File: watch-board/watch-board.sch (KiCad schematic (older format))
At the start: 4 parts

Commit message: setting up linear voltage regulator at 3.1V
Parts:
- removed Q?: Transistor-BJT_MMBT3904-TP, Package_TO_SOT_SMD:SOT-23, symbol luke:Transistor-BJT_MMBT3904-TP
- added C?: C_4.7uF, Capacitor_SMD:C_1206_3216Metric, symbol luke:C_4.7uF
- added C?: C_7pF, Capacitor_SMD:C_0805_2012Metric, symbol luke:C_7pF
- added C?: C_1uF, Capacitor_SMD:C_0805_2012Metric, symbol luke:C_1uF
- added Q?: Transistor_MMBT3904-TP, Package_TO_SOT_SMD:SOT-23, symbol luke:Transistor_MMBT3904-TP
- added R?: R_51.1K, Resistor_SMD:R_0805_2012Metric, symbol luke:R_51.1K
- added R?: R_78.7K, Resistor_SMD:R_0805_2012Metric, symbol luke:R_78.7K
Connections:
- net labels added: GND
- wire segments 0 -> 15
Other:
- note added: "Vout = Vref + (Vref * (Radj/51.1K))\nVref Typical = 1.225 (min = 1.213 max = 1.237)\nRadj = 78.7K\nVout =3.11\n3.08 < Vout < 3.14"
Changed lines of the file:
@@
 $EndComp
 $Comp
-L luke:Transistor-BJT_MMBT3904-TP Q?
-U 1 1 5EA1FA57
-P 5250 4500
-F 0 "Q?" H 5440 4546 50  0000 L CNN
-F 1 "Transistor-BJT_MMBT3904-TP" H 5440 4455 50  0000 L CNN
-F 2 "Package_TO_SOT_SMD:SOT-23" H 5450 4425 50  0001 L CIN
-F 3 "https://www.mccsemi.com/pdf/Products/MMBT3904(SOT-23).pdf" H 5250 4500 50  0001 L CNN
-F 4 "https://www.digikey.com/product-detail/en/micro-commercial-co/MMBT3904-TP/MMBT3904TPMSCT-ND/717395" H 5250 4500 50  0001 L CNN "Purchasing Link"
-F 5 "MMBT3904TPMSCT-ND " H 5250 4500 50  0001 L CNN "Digi-Key_PN"
-	1    5250 4500
+L luke:Transistor_MMBT3904-TP Q?
+U 1 1 5EA32A90
+P 5350 4400
+F 0 "Q?" H 5540 4446 50  0000 L CNN
+F 1 "Transistor_MMBT3904-TP" H 5540 4355 50  0000 L CNN
+F 2 "Package_TO_SOT_SMD:SOT-23" H 5550 4300 50  0001 L CIN
+F 3 "https://www.mccsemi.com/pdf/Products/MMBT3904(SOT-23).pdf" H 5350 4400 50  0001 L CNN
+F 4 "https://www.digikey.com/product-detail/en/micro-commercial-co/MMBT3904-TP/MMBT3904TPMSCT-ND/717395" H 5550 4200 50  0001 L CNN "Purchasing Link"
+F 5 "MMBT3904TPMSCT-ND " H 5550 4100 50  0001 L CNN "Digi-Key_PN"
+	1    5350 4400
 	1    0    0    -1
 $EndComp
+$Comp
+L luke:C_4.7uF C?
+U 1 1 5EA337B8
+P 7700 1550
+F 0 "C?" H 7815 1596 50  0000 L CNN
+F 1 "C_4.7uF" H 7815 1505 50  0000 L CNN
+F 2 "Capacitor_SMD:C_1206_3216Metric" H 7700 900 50  0001 C CNN
+F 3 "http://datasheets.avx.com/TAJ.pdf" H 7725 1650 50  0001 C CNN
+F 4 "478-3868-2-ND " H 7700 1000 60  0001 C CNN "Digi-Key_PN"
+F 5 "https://www.digikey.com/product-detail/en/avx-corporation/TAJA475K016RNJ/478-3868-2-ND/1126796" H 7700 800 60  0001 C CNN "Purchasing Link"
+	1    7700 1550
+	1    0    0    -1
+$EndComp
+$Comp
+L power:GND #PWR?
+U 1 1 5EA36173
+P 7700 1700
+F 0 "#PWR?" H 7700 1450 50  0001 C CNN
+F 1 "GND" H 7705 1527 50  0000 C CNN
+F 2 "" H 7700 1700 50  0001 C CNN
+F 3 "" H 7700 1700 50  0001 C CNN
+	1    7700 1700
+	1    0    0    -1
+$EndComp
+$Comp
+L luke:C_7pF C?
+U 1 1 5EA3DC50
+P 7200 1550
+F 0 "C?" H 7315 1596 50  0000 L CNN
+F 1 "C_7pF" H 7315 1505 50  0000 L CNN
+F 2 "Capacitor_SMD:C_0805_2012Metric" H 7238 1400 50  0001 C CNN
+F 3 "http://datasheets.avx.com/C0GNP0-Dielectric.pdf" H 7225 1650 50  0001 C CNN
+F 4 "478-10543-1-ND" H 7200 1550 60  0001 C CNN "Digi-Key_PN"
+F 5 "https://www.digikey.com/product-detail/en/avx-corporation/08055A7R0CAT2A/478-10543-1-ND/6797474" H 7625 2050 60  0001 C CNN "Purchasing Link"
+	1    7200 1550
+	1    0    0    -1
+$EndComp
+Text Notes 5450 2900 0    50   ~ 0
+Vout = Vref + (Vref * (Radj/51.1K))\nVref Typical = 1.225 (min = 1.213 max = 1.237)\nRadj = 78.7K\nVout =3.11\n3.08 < Vout < 3.14
+$Comp
+L power:GND #PWR?
+U 1 1 5EA5975A
+P 6600 2100
+F 0 "#PWR?" H 6600 1850 50  0001 C CNN
+F 1 "GND" H 6605 1927 50  0000 C CNN
+F 2 "" H 6600 2100 50  0001 C CNN
+F 3 "" H 6600 2100 50  0001 C CNN
+	1    6600 2100
+	1    0    0    -1
+$EndComp
+$Comp
+L luke:R_51.1K R?
+U 1 1 5EA4966E
+P 6600 1950
+F 0 "R?" H 6670 1996 50  0000 L CNN
+F 1 "R_51.1K" H 6670 1905 50  0000 L CNN
+F 2 "Resistor_SMD:R_0805_2012Metric" H 5500 2250 50  0001 L CNN
+F 3 "https://industrial.panasonic.com/cdbs/www-data/pdf/RDA0000/AOA0000C304.pdf" H 5500 2350 50  0001 L CNN
+F 4 "P51.1KCCT-ND" H 5500 2150 60  0001 L CNN "Digi-Key_PN"
+F 5 "https://www.digikey.com/product-detail/en/panasonic-electronic-components/ERJ-6ENF5112V/P51.1KCCT-ND/119466" H 5500 2450 60  0001 L CNN "Purchasing Link"
+	1    6600 1950
+	1    0    0    -1
+$EndComp
+$Comp
+L luke:R_78.7K R?
+U 1 1 5EA619B4
+P 6600 1550
+F 0 "R?" H 6670 1596 50  0000 L CNN
+F 1 "R_78.7K" H 6670 1505 50  0000 L CNN
+F 2 "Resistor_SMD:R_0805_2012Metric" H 5500 1850 50  0001 L CNN
+F 3 "https://www.yageo.com/upload/media/product/productsearch/datasheet/rchip/PYu-RC_Group_51_RoHS_L_10.pdf" H 5500 1950 50  0001 L CNN
+F 4 "311-78.7KCRCT-ND " H 5500 1750 60  0001 L CNN "Digi-Key_PN"
+F 5 "https://www.digikey.com/product-detail/en/yageo/RC0805FR-0778K7L/311-78-7KCRCT-ND/731088" H 5500 2050 60  0001 L CNN "Purchasing Link"
+	1    6600 1550
+	1    0    0    -1
+$EndComp
+Wire Wire Line
+	6600 1700 6600 1750
+Wire Wire Line
+	6600 1750 6350 1750
+Wire Wire Line
+	6350 1450 6300 1450
+Wire Wire Line
+	6600 1750 6600 1800
+Connection ~ 6600 1750
+Wire Wire Line
+	7200 1700 7200 1750
+Wire Wire Line
+	7200 1750 6600 1750
+Wire Wire Line
+	6300 1350 6600 1350
+Wire Wire Line
+	6350 1450 6350 1750
+Wire Wire Line
+	6600 1400 6600 1350
+Connection ~ 6600 1350
+Wire Wire Line
+	6600 1350 7200 1350
+Wire Wire Line
+	7200 1350 7200 1400
+Wire Wire Line
+	7200 1350 7700 1350
+Wire Wire Line
+	7700 1350 7700 1400
+Connection ~ 7200 1350
+$Comp
+L power:GND #PWR?
+U 1 1 5EA7CD31
+P 5900 1750
+F 0 "#PWR?" H 5900 1500 50  0001 C CNN
+F 1 "GND" H 5905 1577 50  0000 C CNN
+F 2 "" H 5900 1750 50  0001 C CNN
+F 3 "" H 5900 1750 50  0001 C CNN
+	1    5900 1750
+	1    0    0    -1
+$EndComp
+$Comp
+L luke:C_1uF C?
+U 1 1 5EA86DAA
+P 4900 1600
+F 0 "C?" H 5015 1696 50  0000 L CNN
+F 1 "C_1uF" H 5015 1605 50  0000 L CNN
+F 2 "Capacitor_SMD:C_0805_2012Metric" H 4938 2200 50  0001 C CNN
+F 3 "https://www.yageo.com/upload/media/product/productsearch/datasheet/mlcc/UPY-GPHC_Y5V_6.3V-to-50V_9.pdf" H 4925 2450 50  0001 C CNN
+F 4 "https://www.digikey.com/product-detail/en/yageo/CC0805ZKY5V9BB105/311-1909-1-ND/5195811#images" H 5325 2100 60  0001 C CNN "Purchasing Link"
+F 5 "311-1909-1-ND " H 4900 2300 50  0001 C CNN "Digi-Key_PN"
+	1    4900 1600
+	1    0    0    -1
+$EndComp
+Wire Wire Line
+	5500 1350 4900 1350
+Wire Wire Line
+	4900 1350 4900 1400
+$Comp
+L power:GND #PWR?
+U 1 1 5EA88D89
+P 4900 1700
+F 0 "#PWR?" H 4900 1450 50  0001 C CNN
+F 1 "GND" H 4905 1527 50  0000 C CNN
+F 2 "" H 4900 1700 50  0001 C CNN
+F 3 "" H 4900 1700 50  0001 C CNN
+	1    4900 1700
+	1    0    0    -1
+$EndComp

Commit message: adding battery and solar cell
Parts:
- added BT?: BAT_ML2020, symbol luke:BAT_ML2020
- added D? (x2): D-Schotkey_BAT54HT1G, Diode_SMD:D_SOD-323, symbol luke:D-Schotkey_BAT54HT1G
- added R?: R_160, Resistor_SMD:R_0805_2012Metric, symbol luke:R_160
- added R?: R_2.21M, Resistor_SMD:R_0805_2012Metric, symbol luke:R_2.21M
- added SC?: Solar-Cells_KXOB25-02X8F, symbol luke:Solar-Cells_KXOB25-02X8F
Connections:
- net labels added: VCC, V_BAT, V_Charge
- wire segments 15 -> 30
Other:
- note added: "Calcular ESR is 886Ohms\n160Ohm resistor used for current limiting durring charging"
- moved on the sheet: C?, R?, U?

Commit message: power management desgin complete
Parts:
- removed Q?: Transistor_MMBT3904-TP, Package_TO_SOT_SMD:SOT-23, symbol luke:Transistor_MMBT3904-TP
- removed R?: R_2.21M, Resistor_SMD:R_0805_2012Metric, symbol luke:R_2.21M
- added D?: D-Schotkey_BAT54HT1G, Diode_SMD:D_SOD-323, symbol luke:D-Schotkey_BAT54HT1G
- added Q?: Transistor_FZT796ATA, Package_TO_SOT_SMD:SOT-223, symbol luke:Transistor_FZT796ATA
- added R?: R_100K, Resistor_SMD:R_0805_2012Metric, symbol luke:R_100K
- added R?: R_200K, Resistor_SMD:R_0805_2012Metric, symbol luke:R_200K
- added R?: R_1.2M, Resistor_SMD:R_0805_2012Metric, symbol luke:R_1.2M
- added R?: R_49.9K, Resistor_SMD:R_0805_2012Metric, symbol luke:R_49.9K
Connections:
- net labels added: V_Charge_ON
- wire segments 30 -> 46
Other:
- note added: "Rt = 1500000 (high value for low current draw)\nR3 = (Rt/Vo)*Vi\nR2 = ((Rt/Vu)*(Vi-Vhys))-R3\nR1 = Rt - R2 - R3\nVi = 0.4V\nVo = 3V\nVu = 2V\nVhys = 5.5mV [(Vi+) - (Vi-)]\n\nR2 =95875 (rounding up to 100K for convience)\nR3 = 200K"
- moved on the sheet: BT?, C?, D?, R?, SC?, U?

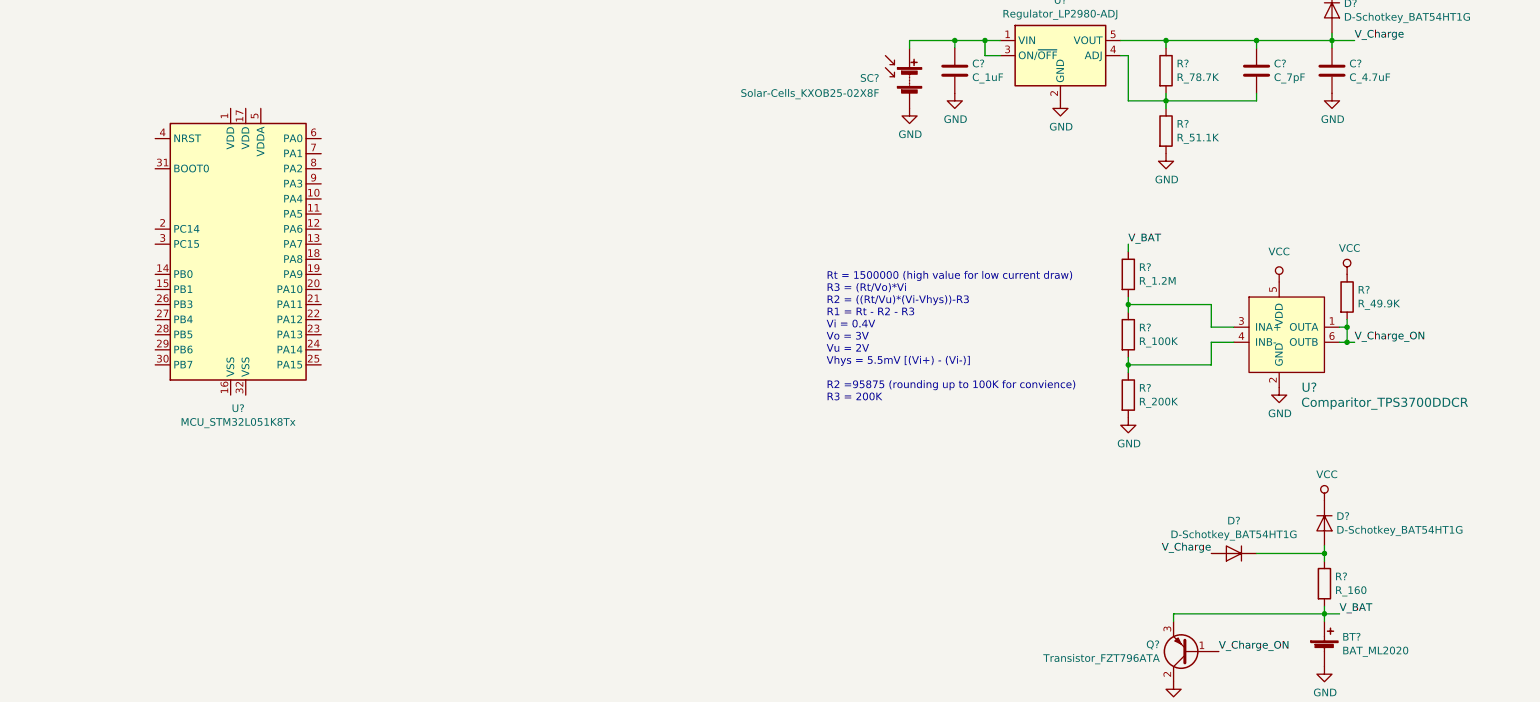
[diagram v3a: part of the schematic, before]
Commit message: adding bypass caps to STM32
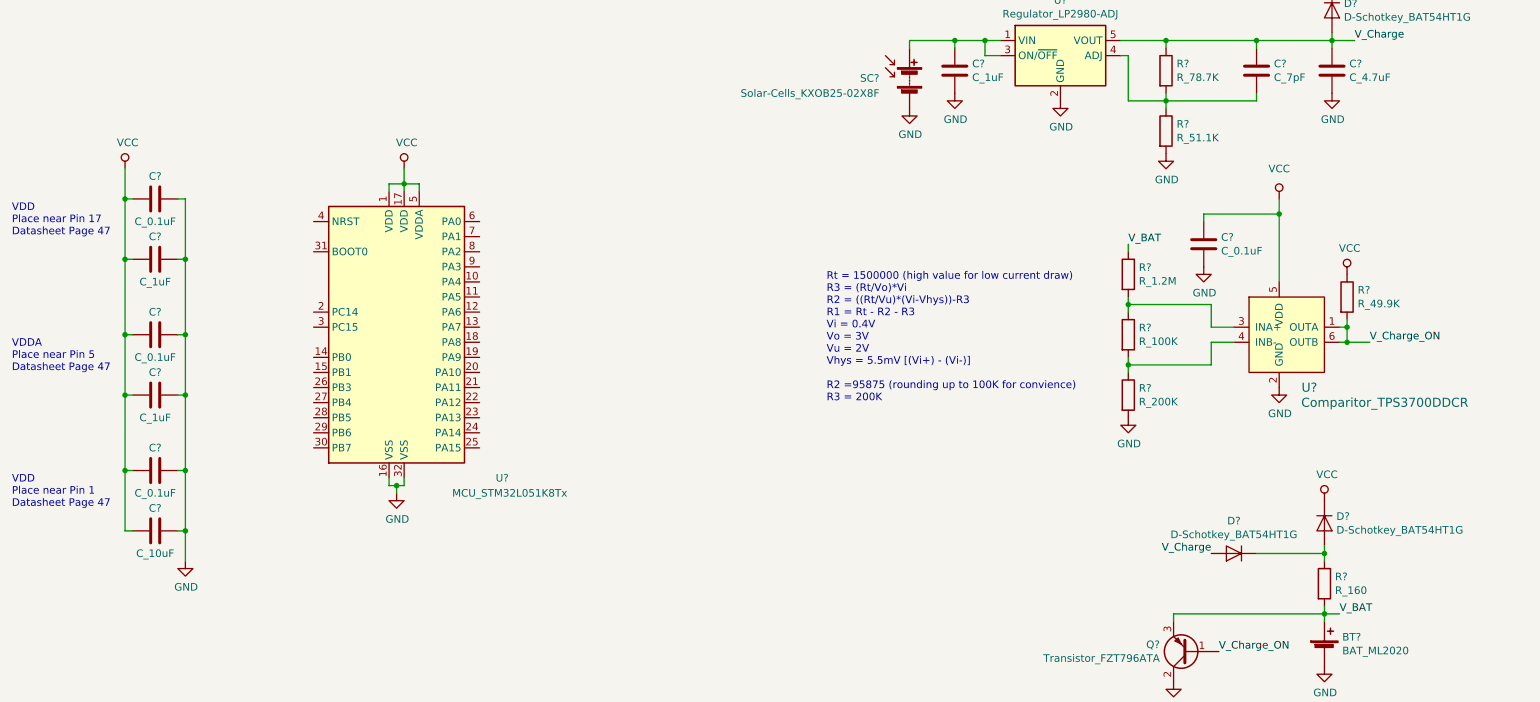
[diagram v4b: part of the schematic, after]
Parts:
- added C? (x4): C_0.1uF, Capacitor_SMD:C_0805_2012Metric, symbol luke:C_0.1uF
- added C? (x2): C_1uF, Capacitor_SMD:C_0805_2012Metric, symbol luke:C_1uF
- added C?: C_10uF, Capacitor_SMD:C_0805_2012Metric, symbol luke:C_10uF
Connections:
- net GND: now also U?.16 (VSS), U?.32 (VSS), C?.1, C?.1, C?.1, C?.1, C?.1, C?.1, C?.1
- net VCC: now also U?.1 (VDD), U?.17 (VDD), U?.5 (VDDA), C?.2, C?.2, C?.2, C?.2, C?.2, C?.2, C?.2
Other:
- note added: "VDDA\nPlace near Pin 5\nDatasheet Page 47"
- note added: "VDD\nPlace near Pin 17\nDatasheet Page 47"
- note added: "VDD\nPlace near Pin 1\nDatasheet Page 47"
- moved on the sheet: U?

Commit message: adding TODOs
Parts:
- added C?: C_0.1uF, Capacitor_SMD:C_0805_2012Metric, symbol luke:C_0.1uF
- added J?: Conn_01x05_Male, Connector_PinHeader_2.54mm:PinHeader_1x05_P2.54mm_Vertical, symbol luke:Conn_01x05_Male
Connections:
- net GND: now also U?.31 (BOOT0), C?.2, J?.4 (Pin_4)
- net VCC: no longer C?.2, C?.2, C?.2, C?.2, C?.2, C?.2, C?.2, R?.1, U?.1 (VDD), U?.17 (VDD), U?.5 (VDD), U?.5 (VDDA)
- net V_BAT: no longer Q?.3 (E)
- net V_Charge: now also Q?.3 (E), R?.1
- net SWDIO: now reaches U?.23 (PA13)
- net SWDIO: now also J?.3 (Pin_3)
- net SWCLK: now reaches U?.24 (PA14)
- net SWCLK: now also J?.2 (Pin_2)
- net RST: now reaches U?.4 (NRST)
- net RST: now also C?.1, J?.1 (Pin_1)
- new net VDD: C?.2, C?.2, C?.2, C?.2, C?.2, C?.2, C?.2, J?.5 (Pin_5), U?.1 (VDD), U?.17 (VDD), U?.5 (VDD), U?.5 (VDDA)
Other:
- note added: "Add SPI Pins"
- note added: "use BUCK-BOOST (TPS6305) to set VDD to 3V"
- moved on the sheet: C?, D?, Q?, R?, SC?, U?

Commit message: adding more TODOs
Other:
- note added: "TODO: Add SPI Pins"
- note removed: "Add SPI Pins"
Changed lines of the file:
@@
 $EndComp
 Text Notes 5500 5450 0    50   ~ 0
-Add SPI Pins
+TODO: Add SPI Pins
 $EndSCHEMATC

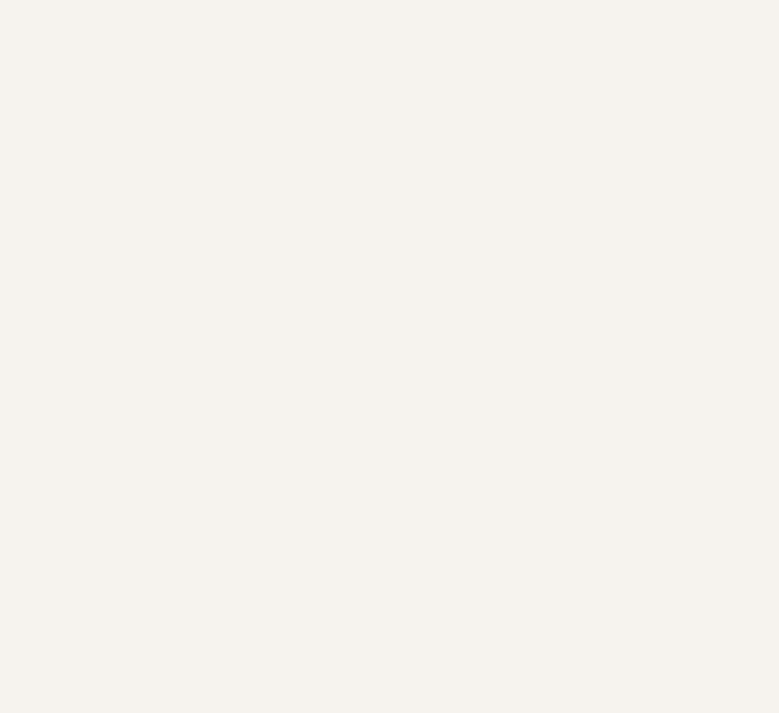
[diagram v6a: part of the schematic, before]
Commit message: switching to LTC3105 for power harvesting
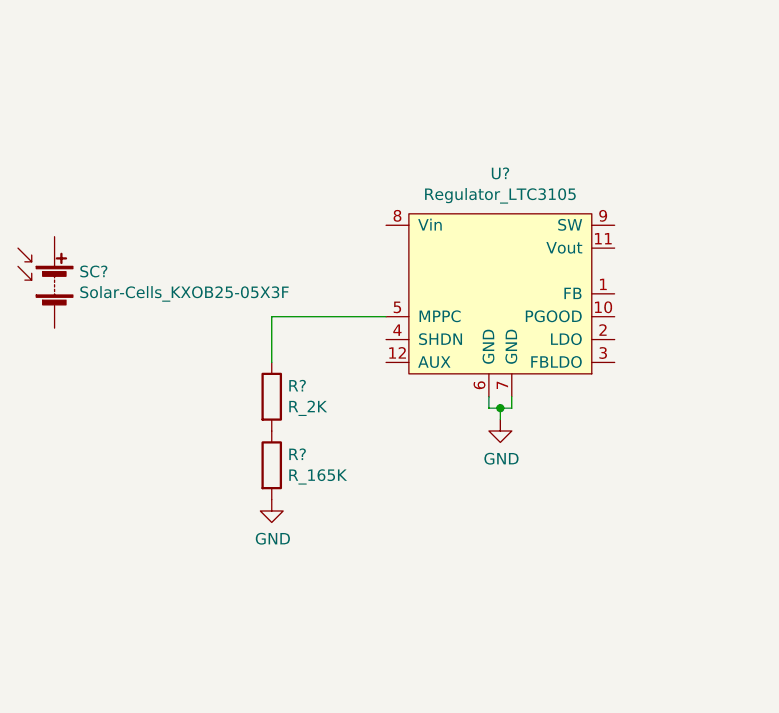
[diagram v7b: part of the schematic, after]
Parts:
- added R?: R_2K, Resistor_SMD:R_0805_2012Metric, symbol luke:R_2K
- added R?: R_165K, Resistor_SMD:R_0805_2012Metric, symbol luke:R_165K
- added SC?: Solar-Cells_KXOB25-05X3F, symbol luke:Solar-Cells_KXOB25-05X3F
- added U?: Regulator_LTC3105, Digikey-footprints:MSOP-12-1EP_W3mm, symbol luke:Regulator_LTC3105
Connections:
- net GND: now also R?.2, U?.6 (GND), U?.7 (GND)
- new net: R?.1, U?.5 (MPPC)
- new net: R?.1, R?.2
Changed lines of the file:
@@
 Text Notes 5500 5450 0    50   ~ 0
 TODO: Add SPI Pins
+$Comp
+L luke:Regulator_LTC3105 U?
+U 1 1 5EBDFA52
+P -3600 2050
+F 0 "U?" H -3600 2575 50  0000 C CNN
+F 1 "Regulator_LTC3105" H -3600 2484 50  0000 C CNN
+F 2 "Digikey-footprints:MSOP-12-1EP_W3mm" H -3600 1150 50  0001 C CNN
+F 3 "https://www.analog.com/media/en/technical-documentation/data-sheets/3105fb.pdf" H -3600 2900 50  0001 C CNN
+F 4 "LTC3105EMS#PBF-ND" H -3600 1350 50  0001 C CNN "Digi-Key_PN"
+F 5 "https://www.digikey.com/product-detail/en/LTC3105EMS%23PBF/LTC3105EMS%23PBF-ND/2601181" H -3600 1250 50  0001 C CNN "Purchasing Link"
+	1    -3600 2050
+	1    0    0    -1
+$EndComp
+$Comp
+L luke:Solar-Cells_KXOB25-05X3F SC?
+U 1 1 5EBE50EA
+P -5550 2000
+F 0 "SC?" H -5442 2046 50  0000 L CNN
+F 1 "Solar-Cells_KXOB25-05X3F" H -5442 1955 50  0000 L CNN
+F 2 "" V -5550 2060 50  0001 C CNN
+F 3 "https://ixapps.ixys.com/DataSheet/KXOB25_05X3F.pdf" V -5550 2060 50  0001 L CNN
+F 4 "KXOB25-05X3FCT-ND" H -5450 1900 50  0001 L CNN "Digi-Key_PN"
+F 5 "https://www.digikey.com/product-detail/en/ixys/KXOB25-05X3F-TR/KXOB25-05X3FCT-ND/9990481" H -5450 1800 50  0001 L CNN "Purchasing Link"
+	1    -5550 2000
+	1    0    0    -1
+$EndComp
+$Comp
+L luke:R_2K R?
+U 1 1 5EBE7BEB
+P -4600 2500
+F 0 "R?" H -4530 2546 50  0000 L CNN
+F 1 "R_2K" H -4530 2455 50  0000 L CNN
+F 2 "Resistor_SMD:R_0805_2012Metric" H -5700 2800 50  0001 L CNN
+F 3 "https://www.yageo.com/upload/media/product/productsearch/datasheet/rchip/PYu-RC_Group_51_RoHS_L_10.pdf" H -5700 2900 50  0001 L CNN
+F 4 "311-2.00KCRCT-ND" H -5700 2700 60  0001 L CNN "Digi-Key_PN"
+F 5 "https://www.digikey.com/product-detail/en/yageo/RC0805FR-072KL/311-2-00KCRCT-ND/730611" H -5700 3000 60  0001 L CNN "Purchasing Link"
+	1    -4600 2500
+	1    0    0    -1
+$EndComp
+$Comp
+L luke:R_165K R?
+U 1 1 5EBE80D7
+P -4600 2800
+F 0 "R?" H -4530 2846 50  0000 L CNN
+F 1 "R_165K" H -4530 2755 50  0000 L CNN
+F 2 "Resistor_SMD:R_0805_2012Metric" H -5700 3100 50  0001 L CNN
+F 3 "https://www.yageo.com/upload/media/product/productsearch/datasheet/rchip/PYu-RC_Group_51_RoHS_L_10.pdf" H -5700 3200 50  0001 L CNN
+F 4 "311-165KCRCT-ND" H -5700 3000 60  0001 L CNN "Digi-Key_PN"
+F 5 "https://www.digikey.com/product-detail/en/yageo/RC0805FR-07165KL/311-165KCRCT-ND/730579" H -5700 3300 60  0001 L CNN "Purchasing Link"
+	1    -4600 2800
+	1    0    0    -1
+$EndComp
+$Comp
+L power:GND #PWR?
+U 1 1 5EBE95AC
+P -4600 2950
+F 0 "#PWR?" H -4600 2700 50  0001 C CNN
+F 1 "GND" H -4595 2777 50  0000 C CNN
+F 2 "" H -4600 2950 50  0001 C CNN
+F 3 "" H -4600 2950 50  0001 C CNN
+	1    -4600 2950
+	1    0    0    -1
+$EndComp
+Wire Wire Line
+	-4100 2150 -4600 2150
+Wire Wire Line
+	-4600 2150 -4600 2350
+$Comp
+L power:GND #PWR?
+U 1 1 5EBEE5DA
+P -3600 2600
+F 0 "#PWR?" H -3600 2350 50  0001 C CNN
+F 1 "GND" H -3595 2427 50  0000 C CNN
+F 2 "" H -3600 2600 50  0001 C CNN
+F 3 "" H -3600 2600 50  0001 C CNN
+	1    -3600 2600
+	1    0    0    -1
+$EndComp
+Wire Wire Line
+	-3550 2500 -3550 2550
+Wire Wire Line
+	-3550 2550 -3600 2550
+Wire Wire Line
+	-3650 2550 -3650 2500
+Wire Wire Line
+	-3600 2550 -3600 2600
+Connection ~ -3600 2550
+Wire Wire Line
+	-3600 2550 -3650 2550
 $EndSCHEMATC
